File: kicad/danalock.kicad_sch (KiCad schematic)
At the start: 10 parts, among them J1 Conn_02x02_Top_Bottom, M1 Motor_DC, SW1 Rotary_Encoder, U1 WeMos_D1_mini, U2 HW-133, U3 TB6612FNG_Module

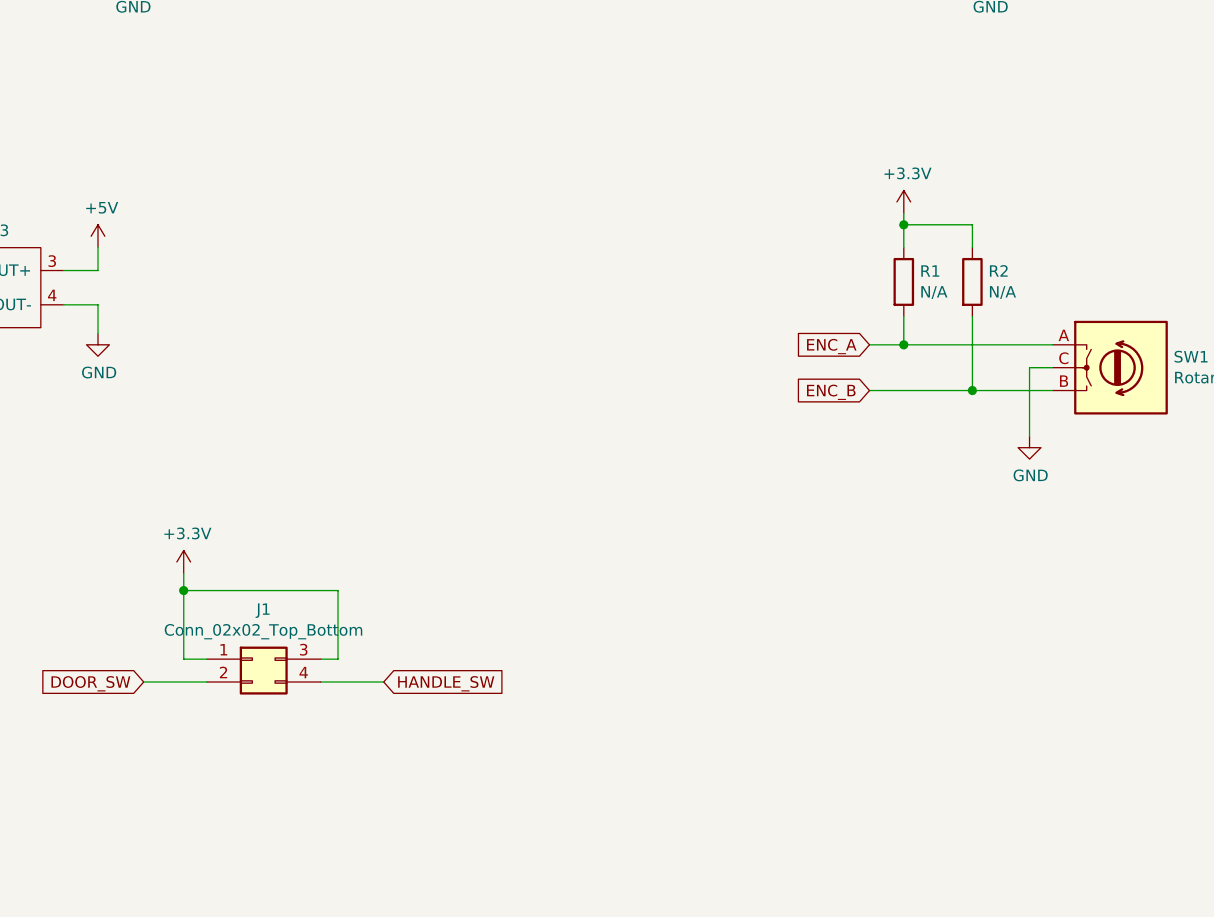
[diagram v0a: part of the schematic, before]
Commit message: The ESP8266 does not support internal pulldown, so use external pulldown for switch inputs.
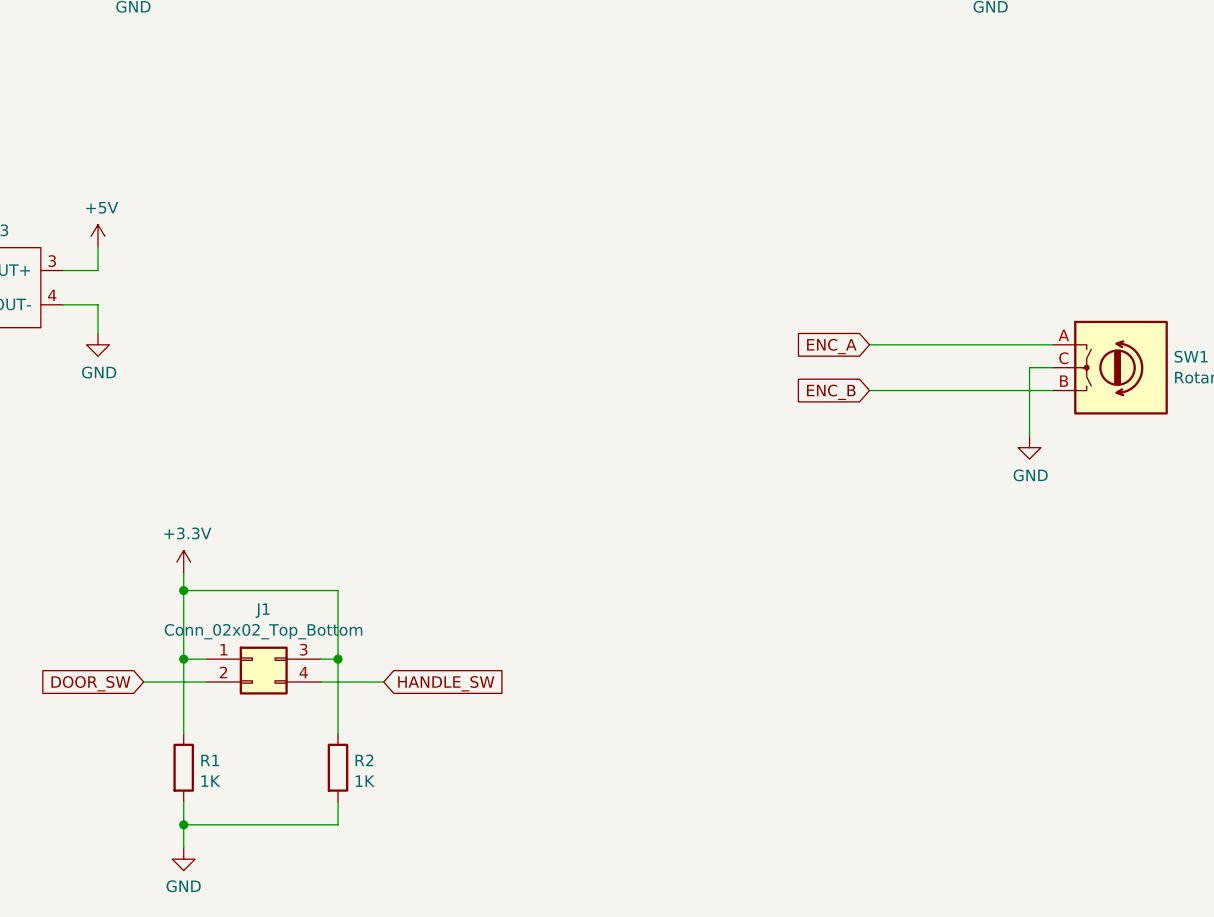
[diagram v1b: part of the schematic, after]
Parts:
- R1, R2: value N/A -> 1K
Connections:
- net ENC_A: no longer R1.2
- net ENC_B: no longer R2.2
- net GND: now also R1.2, R2.2
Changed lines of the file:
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@@
   (paper "A4")
   (junction (at 107.315 154.94) (diameter 1.016) (color 0 0 0 0))
-  (junction (at 187.325 114.3) (diameter 1.016) (color 0 0 0 0))
-  (junction (at 187.325 127.635) (diameter 1.016) (color 0 0 0 0))
-  (junction (at 194.945 132.715) (diameter 1.016) (color 0 0 0 0))
+  (junction (at 107.315 162.56) (diameter 1.016) (color 0 0 0 0))
+  (junction (at 107.315 180.975) (diameter 1.016) (color 0 0 0 0))
+  (junction (at 124.46 162.56) (diameter 1.016) (color 0 0 0 0))
   (no_connect (at 71.12 61.595))
   (no_connect (at 71.12 64.135))
@@
     (stroke (width 0) (type solid) (color 0 0 0 0))
   )
+  (wire (pts (xy 107.315 162.56) (xy 107.315 170.815))
+    (stroke (width 0) (type solid) (color 0 0 0 0))
+  )
   (wire (pts (xy 107.315 162.56) (xy 109.855 162.56))
     (stroke (width 0) (type solid) (color 0 0 0 0))
   )
+  (wire (pts (xy 107.315 178.435) (xy 107.315 180.975))
+    (stroke (width 0) (type solid) (color 0 0 0 0))
+  )
+  (wire (pts (xy 107.315 180.975) (xy 107.315 183.515))
+    (stroke (width 0) (type solid) (color 0 0 0 0))
+  )
   (wire (pts (xy 109.855 165.1) (xy 102.87 165.1))
     (stroke (width 0) (type solid) (color 0 0 0 0))
@@
     (stroke (width 0) (type solid) (color 0 0 0 0))
   )
+  (wire (pts (xy 124.46 162.56) (xy 124.46 170.815))
+    (stroke (width 0) (type solid) (color 0 0 0 0))
+  )
+  (wire (pts (xy 124.46 178.435) (xy 124.46 180.975))
+    (stroke (width 0) (type solid) (color 0 0 0 0))
+  )
+  (wire (pts (xy 124.46 180.975) (xy 107.315 180.975))
+    (stroke (width 0) (type solid) (color 0 0 0 0))
+  )
   (wire (pts (xy 129.54 165.1) (xy 122.555 165.1))
     (stroke (width 0) (type solid) (color 0 0 0 0))
@@
     (stroke (width 0) (type solid) (color 0 0 0 0))
   )
-  (wire (pts (xy 183.515 132.715) (xy 194.945 132.715))
-    (stroke (width 0) (type solid) (color 0 0 0 0))
-  )
-  (wire (pts (xy 187.325 113.03) (xy 187.325 114.3))
-    (stroke (width 0) (type solid) (color 0 0 0 0))
-  )
-  (wire (pts (xy 187.325 114.3) (xy 187.325 116.84))
-    (stroke (width 0) (type solid) (color 0 0 0 0))
-  )
-  (wire (pts (xy 187.325 124.46) (xy 187.325 127.635))
-    (stroke (width 0) (type solid) (color 0 0 0 0))
-  )
-  (wire (pts (xy 187.325 127.635) (xy 183.515 127.635))
+  (wire (pts (xy 183.515 127.635) (xy 203.835 127.635))
+    (stroke (width 0) (type solid) (color 0 0 0 0))
+  )
+  (wire (pts (xy 183.515 132.715) (xy 203.835 132.715))
     (stroke (width 0) (type solid) (color 0 0 0 0))
   )
@@
     (stroke (width 0) (type solid) (color 0 0 0 0))
   )
-  (wire (pts (xy 194.945 114.3) (xy 187.325 114.3))
-    (stroke (width 0) (type solid) (color 0 0 0 0))
-  )
-  (wire (pts (xy 194.945 116.84) (xy 194.945 114.3))
-    (stroke (width 0) (type solid) (color 0 0 0 0))
-  )
-  (wire (pts (xy 194.945 124.46) (xy 194.945 132.715))
-    (stroke (width 0) (type solid) (color 0 0 0 0))
-  )
-  (wire (pts (xy 194.945 132.715) (xy 203.835 132.715))
-    (stroke (width 0) (type solid) (color 0 0 0 0))
-  )
   (wire (pts (xy 196.85 61.595) (xy 196.85 65.405))
     (stroke (width 0) (type solid) (color 0 0 0 0))
@@
   )
   (wire (pts (xy 201.295 137.795) (xy 201.295 130.175))
-    (stroke (width 0) (type solid) (color 0 0 0 0))
-  )
-  (wire (pts (xy 203.835 127.635) (xy 187.325 127.635))
     (stroke (width 0) (type solid) (color 0 0 0 0))
   )
@@
     (pin "1")
   )
-  (symbol (lib_id "power:+3.3V") (at 187.325 113.03 0) (unit 1)
-    (in_bom yes) (on_board yes)
-    (property "Reference" "#PWR07" (id 0) (at 187.325 116.84 0)
-      (effects (font (size 1.27 1.27)) hide)
-    )
-    (property "Value" "+3.3V" (id 1) (at 187.706 108.6358 0))
-    (property "Footprint" "" (id 2) (at 187.325 113.03 0)
-      (effects (font (size 1.27 1.27)) hide)
-    )
-    (property "Datasheet" "" (id 3) (at 187.325 113.03 0)
-      (effects (font (size 1.27 1.27)) hide)
-    )
-    (pin "1")
-  )
   (symbol (lib_id "power:+3.3V") (at 192.405 55.88 0) (unit 1)
     (in_bom yes) (on_board yes)
@@
     )
     (property "Datasheet" "" (id 3) (at 101.6 85.725 0)
+      (effects (font (size 1.27 1.27)) hide)
+    )
+    (pin "1")
+  )
+  (symbol (lib_id "power:GND") (at 107.315 183.515 0) (unit 1)
+    (in_bom yes) (on_board yes) (fields_autoplaced)
+    (property "Reference" "#PWR07" (id 0) (at 107.315 189.865 0)
+      (effects (font (size 1.27 1.27)) hide)
+    )
+    (property "Value" "GND" (id 1) (at 107.315 187.8394 0))
+    (property "Footprint" "" (id 2) (at 107.315 183.515 0)
+      (effects (font (size 1.27 1.27)) hide)
+    )
+    (property "Datasheet" "" (id 3) (at 107.315 183.515 0)
       (effects (font (size 1.27 1.27)) hide)
     )
@@
     (pin "2")
   )
-  (symbol (lib_id "Device:R") (at 187.325 120.65 0) (unit 1)
-    (in_bom yes) (on_board yes)
-    (property "Reference" "R1" (id 0) (at 189.103 119.4816 0)
+  (symbol (lib_id "Device:R") (at 107.315 174.625 0) (unit 1)
+    (in_bom yes) (on_board yes) (fields_autoplaced)
+    (property "Reference" "R1" (id 0) (at 109.0931 173.8641 0)
       (effects (font (size 1.27 1.27)) (justify left))
     )
-    (property "Value" "N/A" (id 1) (at 189.103 121.793 0)
+    (property "Value" "1K" (id 1) (at 109.0931 176.1628 0)
       (effects (font (size 1.27 1.27)) (justify left))
     )
-    (property "Footprint" "" (id 2) (at 185.547 120.65 90)
-      (effects (font (size 1.27 1.27)) hide)
-    )
-    (property "Datasheet" "~" (id 3) (at 187.325 120.65 0)
-      (effects (font (size 1.27 1.27)) hide)
-    )
-    (pin "1")
-    (pin "2")
-  )
-  (symbol (lib_id "Device:R") (at 194.945 120.65 0) (unit 1)
-    (in_bom yes) (on_board yes)
-    (property "Reference" "R2" (id 0) (at 196.723 119.4816 0)
+    (property "Footprint" "" (id 2) (at 105.537 174.625 90)
+      (effects (font (size 1.27 1.27)) hide)
+    )
+    (property "Datasheet" "~" (id 3) (at 107.315 174.625 0)
+      (effects (font (size 1.27 1.27)) hide)
+    )
+    (pin "1")
+    (pin "2")
+  )
+  (symbol (lib_id "Device:R") (at 124.46 174.625 0) (unit 1)
+    (in_bom yes) (on_board yes) (fields_autoplaced)
+    (property "Reference" "R2" (id 0) (at 126.2381 173.8641 0)
       (effects (font (size 1.27 1.27)) (justify left))
     )
-    (property "Value" "N/A" (id 1) (at 196.723 121.793 0)
+    (property "Value" "1K" (id 1) (at 126.2381 176.1628 0)
       (effects (font (size 1.27 1.27)) (justify left))
     )
-    (property "Footprint" "" (id 2) (at 193.167 120.65 90)
-      (effects (font (size 1.27 1.27)) hide)
-    )
-    (property "Datasheet" "~" (id 3) (at 194.945 120.65 0)
+    (property "Footprint" "" (id 2) (at 122.682 174.625 90)
+      (effects (font (size 1.27 1.27)) hide)
+    )
+    (property "Datasheet" "~" (id 3) (at 124.46 174.625 0)
       (effects (font (size 1.27 1.27)) hide)
     )
@@
       (reference "#PWR06") (unit 1) (value "GND") (footprint "")
     )
-    (path "/00000000-0000-0000-0000-00005fed9bf3"
-      (reference "#PWR07") (unit 1) (value "+3.3V") (footprint "")
+    (path "/a9699b17-bc17-4354-b62d-58d481bda0dc"
+      (reference "#PWR07") (unit 1) (value "GND") (footprint "")
     )
     (path "/00000000-0000-0000-0000-00005fedf1e2"
@@
       (reference "M1") (unit 1) (value "Motor_DC") (footprint "")
     )
-    (path "/00000000-0000-0000-0000-00005fed958b"
-      (reference "R1") (unit 1) (value "N/A") (footprint "")
-    )
-    (path "/00000000-0000-0000-0000-00005fed9029"
-      (reference "R2") (unit 1) (value "N/A") (footprint "")
+    (path "/2efa29db-37dd-45be-8b81-8f16512c4b54"
+      (reference "R1") (unit 1) (value "1K") (footprint "")
+    )
+    (path "/df16ddf0-114d-4b8b-aa51-9fbd10c3b951"
+      (reference "R2") (unit 1) (value "1K") (footprint "")
     )
     (path "/00000000-0000-0000-0000-00005ffe2d2b"

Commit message: Update.
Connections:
- net ENC_A: now also U1.3 (D0); no longer U1.5 (D6)
- net LED: now also U1.5 (D6); no longer U1.3 (D0)
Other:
- note added: "blue"
- note added: "white"
- note added: "yellow"
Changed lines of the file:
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@@
+    (stroke (width 0) (type solid) (color 0 0 0 0))
+  )
+  (wire (pts (xy 96.52 79.375) (xy 120.015 79.375))
     (stroke (width 0) (type solid) (color 0 0 0 0))
   )
@@
     (stroke (width 0) (type solid) (color 0 0 0 0))
   )
-  (wire (pts (xy 114.3 77.47) (xy 114.3 79.375))
-    (stroke (width 0) (type solid) (color 0 0 0 0))
-  )
-  (wire (pts (xy 114.3 79.375) (xy 96.52 79.375))
+  (wire (pts (xy 120.015 79.375) (xy 120.015 77.47))
     (stroke (width 0) (type solid) (color 0 0 0 0))
   )
@@
     (stroke (width 0) (type solid) (color 0 0 0 0))
   )
+  (text "blue" (at 109.22 67.945 0)
+    (effects (font (size 1.27 1.27)) (justify left bottom))
+  )
+  (text "blue" (at 109.22 70.485 0)
+    (effects (font (size 1.27 1.27)) (justify left bottom))
+  )
+  (text "yellow\n" (at 109.22 73.025 0)
+    (effects (font (size 1.27 1.27)) (justify left bottom))
+  )
+  (text "white" (at 109.22 75.565 0)
+    (effects (font (size 1.27 1.27)) (justify left bottom))
+  )
+  (text "yellow\n" (at 247.65 66.04 0)
+    (effects (font (size 1.27 1.27)) (justify left bottom))
+  )
+  (text "blue" (at 247.65 69.215 0)
+    (effects (font (size 1.27 1.27)) (justify left bottom))
+  )
+  (text "blue" (at 247.65 71.755 0)
+    (effects (font (size 1.27 1.27)) (justify left bottom))
+  )
+  (text "white" (at 247.65 74.295 0)
+    (effects (font (size 1.27 1.27)) (justify left bottom))
+  )
   (global_label "LED" (shape input) (at 59.055 160.655 180) (fields_autoplaced)
     (effects (font (size 1.27 1.27)) (justify right))
@@
     )
   )
-  (global_label "LED" (shape input) (at 66.04 66.675 180) (fields_autoplaced)
+  (global_label "ENC_A" (shape input) (at 66.04 66.675 180) (fields_autoplaced)
+    (effects (font (size 1.27 1.27)) (justify right))
+    (property "Intersheet References" "${INTERSHEET_REFS}" (id 0) (at 0 -7.62 0)
+      (effects (font (size 1.27 1.27)) hide)
+    )
+  )
+  (global_label "ENC_B" (shape input) (at 66.04 69.215 180) (fields_autoplaced)
     (effects (font (size 1.27 1.27)) (justify right))
     (property "Intersheet References" "${INTERSHEET_REFS}" (id 0) (at 0 -2.54 0)
@@
     )
   )
-  (global_label "ENC_B" (shape input) (at 66.04 69.215 180) (fields_autoplaced)
-    (effects (font (size 1.27 1.27)) (justify right))
-    (property "Intersheet References" "${INTERSHEET_REFS}" (id 0) (at 0 -2.54 0)
-      (effects (font (size 1.27 1.27)) hide)
-    )
-  )
-  (global_label "ENC_A" (shape input) (at 66.04 71.755 180) (fields_autoplaced)
-    (effects (font (size 1.27 1.27)) (justify right))
-    (property "Intersheet References" "${INTERSHEET_REFS}" (id 0) (at 0 -2.54 0)
+  (global_label "LED" (shape input) (at 66.04 71.755 180) (fields_autoplaced)
+    (effects (font (size 1.27 1.27)) (justify right))
+    (property "Intersheet References" "${INTERSHEET_REFS}" (id 0) (at 0 2.54 0)
       (effects (font (size 1.27 1.27)) hide)
     )
@@
     (pin "1")
   )
-  (symbol (lib_id "power:+5V") (at 114.3 77.47 0) (unit 1)
-    (in_bom yes) (on_board yes)
-    (property "Reference" "#PWR0101" (id 0) (at 114.3 81.28 0)
-      (effects (font (size 1.27 1.27)) hide)
-    )
-    (property "Value" "+5V" (id 1) (at 114.681 73.0758 0))
-    (property "Footprint" "" (id 2) (at 114.3 77.47 0)
-      (effects (font (size 1.27 1.27)) hide)
-    )
-    (property "Datasheet" "" (id 3) (at 114.3 77.47 0)
-      (effects (font (size 1.27 1.27)) hide)
-    )
+  (symbol (lib_id "power:+5V") (at 120.015 77.47 0) (unit 1)
+    (in_bom yes) (on_board yes)
+    (property "Reference" "#PWR0101" (id 0) (at 120.015 81.28 0)
+      (effects (font (size 1.27 1.27)) hide)
+    )
+    (property "Value" "+5V" (id 1) (at 120.396 73.0758 0))
+    (property "Footprint" "" (id 2) (at 120.015 77.47 0)
+      (effects (font (size 1.27 1.27)) hide)
+    )
+    (property "Datasheet" "" (id 3) (at 120.015 77.47 0)
+      (effects (font (size 1.27 1.27)) hide)
+    )
